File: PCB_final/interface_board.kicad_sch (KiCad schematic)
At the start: 116 parts, among them J1 02x30_Shift_Register_Connector, J2 02x30_ADC_Connector, J5 PicoPinSocketB, J6 PicoPinSocketA, U1 74HC595, U10 LM321, U2 74HC595, U3 74HC595, U4 74HC595, U5 74HC595, U6 74HC595, U7 74HC595, U8 MAX11643EEG, U9 MAX11643EEG

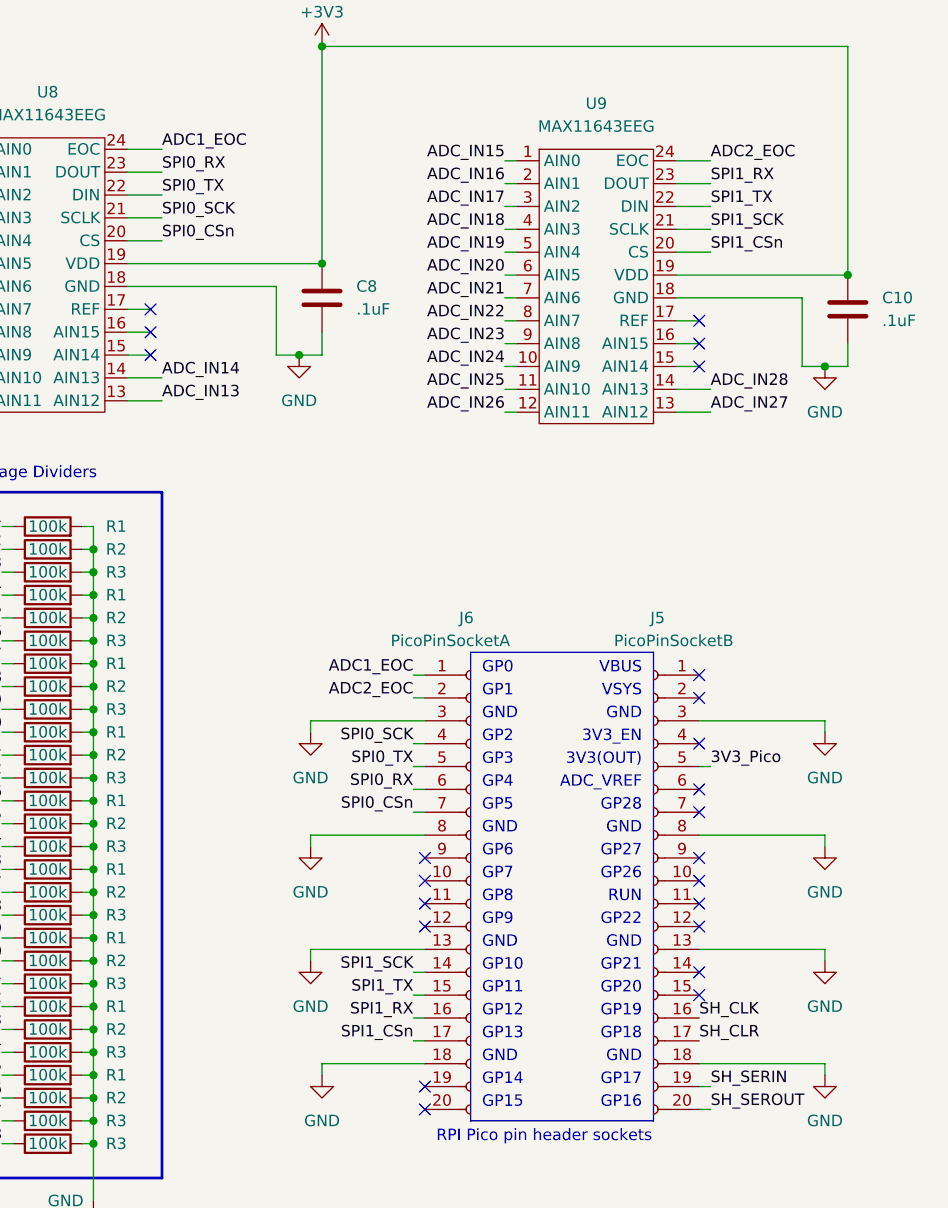
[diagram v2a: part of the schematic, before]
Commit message: Changed to use only one spi channe.
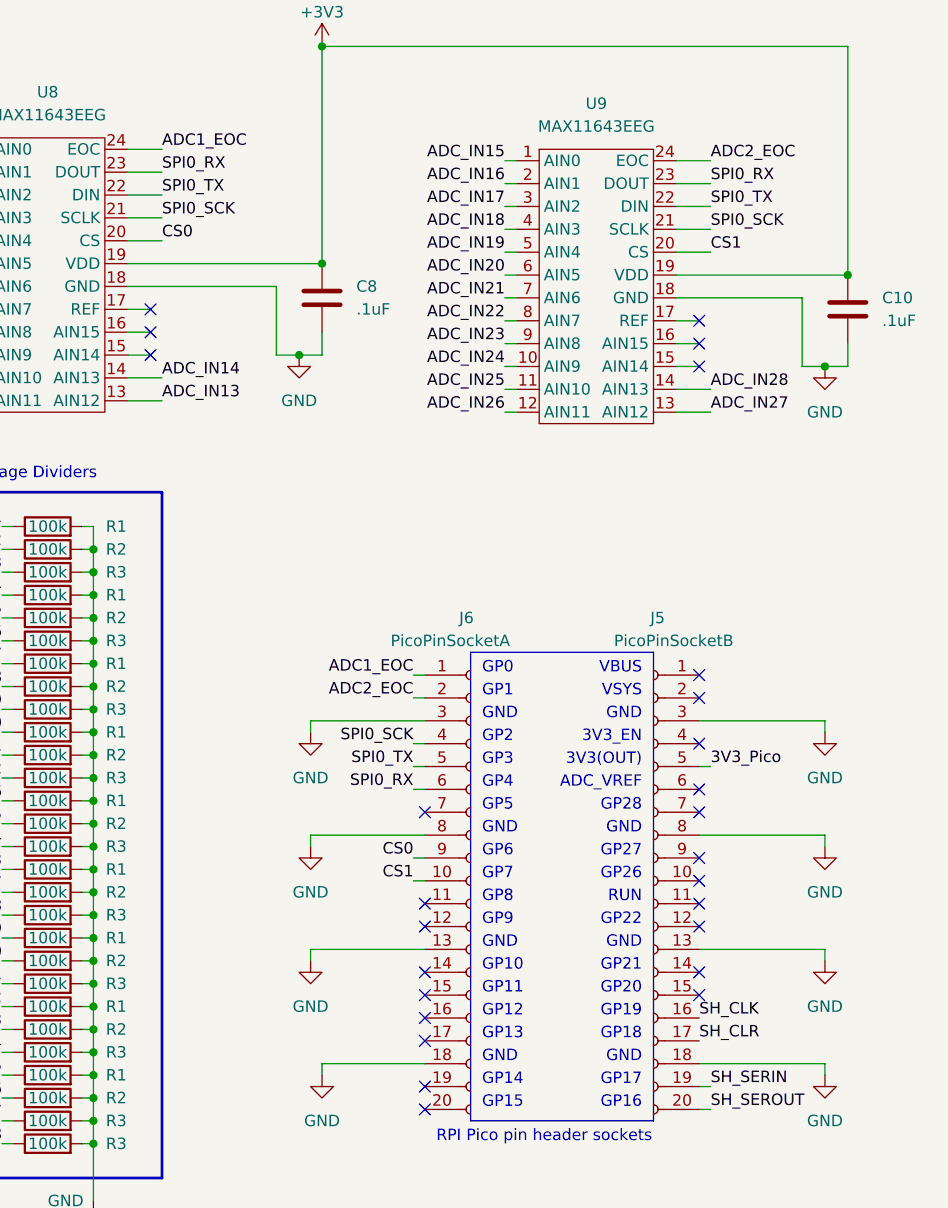
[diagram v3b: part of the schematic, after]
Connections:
- net SPI0_RX: now also U9.23 (DOUT)
- net SPI0_SCK: now also U9.21 (SCLK)
- net SPI0_TX: now also U9.22 (DIN)
- net CS1: now reaches J6.10 (Pin_10)
- net CS1: now also U9.20 (CS)
- net CS0: now reaches J6.9 (Pin_9)
- net CS0: now also U8.20 (CS)
- net SPI0_CSn: no longer names the net of J6.7 (Pin_7)
- net SPI0_CSn: no longer U8.20 (CS)
- net SPI1_CSn: no longer names the net of J6.17 (Pin_17)
- net SPI1_CSn: no longer U9.20 (CS)
- net SPI1_RX: no longer names the net of J6.16 (Pin_16)
- net SPI1_RX: no longer U9.23 (DOUT)
- net SPI1_SCK: no longer names the net of J6.14 (Pin_14)
- net SPI1_SCK: no longer U9.21 (SCLK)
- net SPI1_TX: no longer names the net of J6.15 (Pin_15)
- net SPI1_TX: no longer U9.22 (DIN)
- no-connect marks 59 -> 62
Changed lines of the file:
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@@
   (no_connect (at 199.39 54.61))
   (no_connect (at 132.08 153.67))
-  (no_connect (at 229.87 113.03))
   (no_connect (at 144.78 173.99))
   (no_connect (at 132.08 181.61))
-  (no_connect (at 229.87 110.49))
   (no_connect (at 260.35 102.87))
   (no_connect (at 260.35 97.79))
   (no_connect (at 199.39 52.07))
   (no_connect (at 144.78 163.83))
+  (no_connect (at 229.87 105.41))
+  (no_connect (at 229.87 128.27))
   (no_connect (at 260.35 55.88))
+  (no_connect (at 229.87 125.73))
   (no_connect (at 229.87 115.57))
   (no_connect (at 144.78 168.91))
@@
   (no_connect (at 260.35 105.41))
   (no_connect (at 144.78 166.37))
+  (no_connect (at 229.87 123.19))
   (no_connect (at 132.08 168.91))
   (no_connect (at 132.08 156.21))
@@
   (no_connect (at 260.35 50.8))
   (no_connect (at 144.78 151.13))
+  (no_connect (at 229.87 130.81))
   (no_connect (at 229.87 118.11))
   (no_connect (at 260.35 118.11))
@@
     (stroke (width 0) (type default))
   )
-  (wire (pts (xy 228.6 105.41) (xy 229.87 105.41))
-    (stroke (width 0) (type default))
-  )
   (wire (pts (xy 228.6 92.71) (xy 229.87 92.71))
     (stroke (width 0) (type default))
@@
     (stroke (width 0) (type default))
   )
-  (wire (pts (xy 228.6 125.73) (xy 229.87 125.73))
-    (stroke (width 0) (type default))
-  )
   (wire (pts (xy 153.67 74.93) (xy 154.94 74.93))
     (stroke (width 0) (type default))
@@
     (stroke (width 0) (type default))
   )
-  (wire (pts (xy 228.6 128.27) (xy 229.87 128.27))
+  (wire (pts (xy 228.6 113.03) (xy 229.87 113.03))
     (stroke (width 0) (type default))
   )
@@
     (stroke (width 0) (type default))
   )
-  (wire (pts (xy 228.6 130.81) (xy 229.87 130.81))
-    (stroke (width 0) (type default))
-  )
   (wire (pts (xy 49.53 128.27) (xy 52.07 128.27))
     (stroke (width 0) (type default))
@@
     (stroke (width 0) (type default))
   )
+  (wire (pts (xy 228.6 110.49) (xy 229.87 110.49))
+    (stroke (width 0) (type default))
+  )
   (wire (pts (xy 153.67 57.15) (xy 154.94 57.15))
     (stroke (width 0) (type default))
@@
   )
   (wire (pts (xy 144.78 125.73) (xy 147.32 125.73))
-    (stroke (width 0) (type default))
-  )
-  (wire (pts (xy 228.6 123.19) (xy 229.87 123.19))
     (stroke (width 0) (type default))
   )
@@
     (effects (font (size 1.27 1.27)) (justify right bottom))
   )
-  (label "SPI1_SCK" (at 261.62 40.64 0) (fields_autoplaced)
+  (label "SPI0_SCK" (at 261.62 40.64 0) (fields_autoplaced)
     (effects (font (size 1.27 1.27)) (justify left bottom))
   )
@@
     (effects (font (size 1.27 1.27)) (justify right bottom))
   )
-  (label "SPI1_SCK" (at 228.6 123.19 180) (fields_autoplaced)
-    (effects (font (size 1.27 1.27)) (justify right bottom))
-  )
   (label "SOUT44" (at 154.94 74.93 0) (fields_autoplaced)
     (effects (font (size 1.27 1.27)) (justify left bottom))
@@
     (effects (font (size 1.27 1.27)) (justify left bottom))
   )
-  (label "SPI0_CSn" (at 200.66 41.91 0) (fields_autoplaced)
-    (effects (font (size 1.27 1.27)) (justify left bottom))
-  )
   (label "SOUT18" (at 22.86 107.95 180) (fields_autoplaced)
     (effects (font (size 1.27 1.27)) (justify right bottom))
@@
     (effects (font (size 1.27 1.27)) (justify left bottom))
   )
-  (label "SPI1_RX" (at 261.62 35.56 0) (fields_autoplaced)
+  (label "CS1" (at 228.6 113.03 180) (fields_autoplaced)
+    (effects (font (size 1.27 1.27)) (justify right bottom))
+  )
+  (label "SPI0_RX" (at 261.62 35.56 0) (fields_autoplaced)
     (effects (font (size 1.27 1.27)) (justify left bottom))
   )
@@
     (effects (font (size 1.27 1.27)) (justify right bottom))
   )
-  (label "SPI1_RX" (at 228.6 128.27 180) (fields_autoplaced)
-    (effects (font (size 1.27 1.27)) (justify right bottom))
-  )
   (label "ADC_IN8" (at 182.88 91.44 180) (fields_autoplaced)
     (effects (font (size 1.27 1.27)) (justify right bottom))
   )
-  (label "SPI1_CSn" (at 228.6 130.81 180) (fields_autoplaced)
-    (effects (font (size 1.27 1.27)) (justify right bottom))
-  )
   (label "SOUT53" (at 69.85 115.57 180) (fields_autoplaced)
     (effects (font (size 1.27 1.27)) (justify right bottom))
@@
     (effects (font (size 1.27 1.27)) (justify left bottom))
   )
-  (label "SPI1_CSn" (at 261.62 43.18 0) (fields_autoplaced)
-    (effects (font (size 1.27 1.27)) (justify left bottom))
-  )
   (label "SOUT1" (at 22.86 24.13 180) (fields_autoplaced)
     (effects (font (size 1.27 1.27)) (justify right bottom))
@@
     (effects (font (size 1.27 1.27)) (justify right bottom))
   )
-  (label "SPI1_TX" (at 228.6 125.73 180) (fields_autoplaced)
-    (effects (font (size 1.27 1.27)) (justify right bottom))
-  )
   (label "SOUT40" (at 69.85 41.91 180) (fields_autoplaced)
     (effects (font (size 1.27 1.27)) (justify right bottom))
@@
     (effects (font (size 1.27 1.27)) (justify left bottom))
   )
-  (label "SPI1_TX" (at 261.62 38.1 0) (fields_autoplaced)
+  (label "SPI0_TX" (at 261.62 38.1 0) (fields_autoplaced)
     (effects (font (size 1.27 1.27)) (justify left bottom))
   )
@@
     (effects (font (size 1.27 1.27)) (justify left bottom))
   )
+  (label "CS1" (at 261.62 43.18 0) (fields_autoplaced)
+    (effects (font (size 1.27 1.27)) (justify left bottom))
+  )
   (label "SPI0_RX" (at 228.6 102.87 180) (fields_autoplaced)
     (effects (font (size 1.27 1.27)) (justify right bottom))
@@
     (effects (font (size 1.27 1.27)) (justify right bottom))
   )
+  (label "CS0" (at 200.66 41.91 0) (fields_autoplaced)
+    (effects (font (size 1.27 1.27)) (justify left bottom))
+  )
   (label "ADC2_EOC" (at 228.6 92.71 180) (fields_autoplaced)
     (effects (font (size 1.27 1.27)) (justify right bottom))
@@
     (effects (font (size 1.27 1.27)) (justify right bottom))
   )
+  (label "CS0" (at 228.6 110.49 180) (fields_autoplaced)
+    (effects (font (size 1.27 1.27)) (justify right bottom))
+  )
   (label "ADC_IN20" (at 182.88 121.92 180) (fields_autoplaced)
     (effects (font (size 1.27 1.27)) (justify right bottom))
@@
     (effects (font (size 1.27 1.27)) (justify left bottom))
   )
-  (label "SPI0_CSn" (at 228.6 105.41 180) (fields_autoplaced)
-    (effects (font (size 1.27 1.27)) (justify right bottom))
-  )
   (label "SOUT3" (at 22.86 29.21 180) (fields_autoplaced)

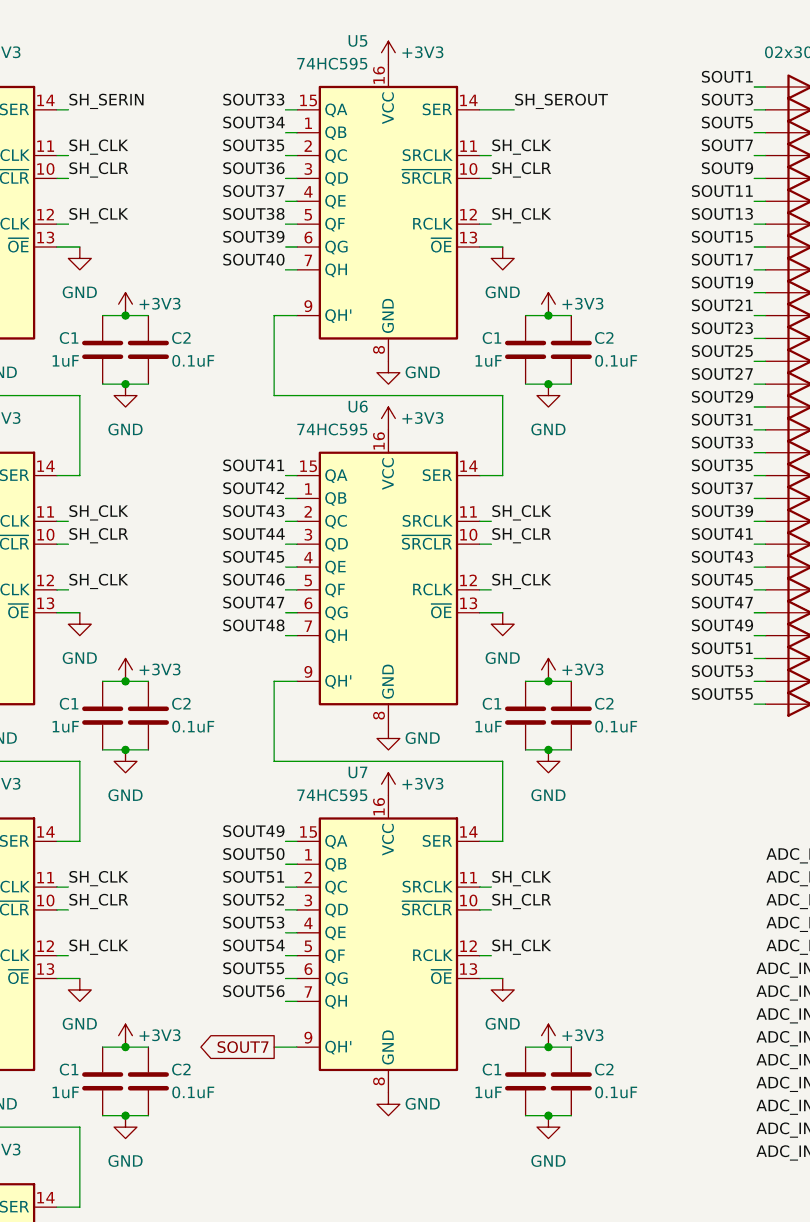
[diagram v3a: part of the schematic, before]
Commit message: Fixed issue in shift register connections
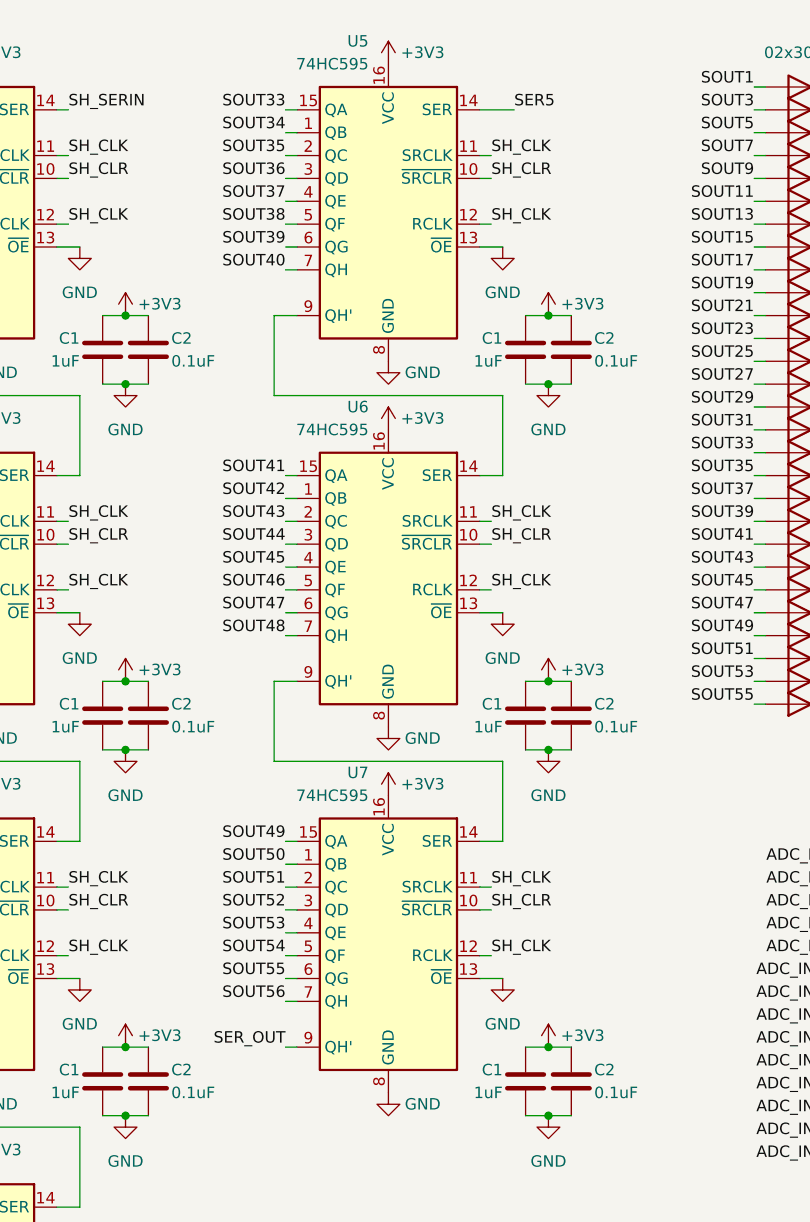
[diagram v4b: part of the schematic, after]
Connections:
- net SER5: now also U5.14 (SER)
- net SH_SEROUT: no longer U5.14 (SER)
- net SOUT7: no longer U7.9 (QH')
- new net SER_OUT: U7.9 (QH')
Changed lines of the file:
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@@
+    (stroke (width 0) (type default))
+  )
+  (wire (pts (xy 69.85 128.27) (xy 71.12 128.27))
     (stroke (width 0) (type default))
   )
@@
   )
   (wire (pts (xy 92.71 31.75) (xy 91.44 31.75))
-    (stroke (width 0) (type default))
-  )
-  (wire (pts (xy 71.12 128.27) (xy 68.58 128.27))
     (stroke (width 0) (type default))
   )
@@
     (effects (font (size 1.27 1.27)) (justify left bottom))
   )
+  (label "SER_OUT" (at 69.85 128.27 180) (fields_autoplaced)
+    (effects (font (size 1.27 1.27)) (justify right bottom))
+  )
   (label "ADC_IN3" (at 179.07 36.83 180) (fields_autoplaced)
     (effects (font (size 1.27 1.27)) (justify right bottom))
@@
     (effects (font (size 1.27 1.27)) (justify left bottom))
   )
-  (label "SH_SEROUT" (at 95.25 24.13 0) (fields_autoplaced)
+  (label "SER5" (at 95.25 24.13 0) (fields_autoplaced)
     (effects (font (size 1.27 1.27)) (justify left bottom))
   )
@@
     (effects (font (size 1.27 1.27)) (justify left bottom))
   )
-  (global_label "SOUT7" (shape output) (at 68.58 128.27 180) (fields_autoplaced)
-    (effects (font (size 1.27 1.27)) (justify right))
-    (property "Intersheetrefs" "${INTERSHEET_REFS}" (at 59.5472 128.27 0)
-      (effects (font (size 1.27 1.27)) (justify right) hide)
-    )
-  )
   (symbol (lib_id "power:+3V3") (at 34.29 140.97 0) (unit 1)
